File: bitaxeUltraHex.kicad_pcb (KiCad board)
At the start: 4 copper layers, 84.5 x 129.5 mm, 333 parts, among them J1 Conn_01x01, J2 Conn_01x01, J3 TC2030-IDC, J4 USB_C_Receptacle_USB2.0, J5 Conn_01x04, J6 Conn_01x04, Q1 NTMFS5C673NLT1G, Q2 CSD17577Q5A, Q3 NTMFS5C673NLT1G, Q4 CSD17577Q5A, Q5 BSS123, SW1 GT-TC029B-H025-L1N, SW2 GT-TC029B-H025-L1N, U1 uA7805, U10 TMP1075, U11 TMP1075, U12 EMC2302, U13 BM1366_mode1, U14 ADP171AUJ-R7, U15 ADP171AUJ-R7, U16 BM1366_mode1, U17 25MHz, U18 TLV3544, U19 BM1366_mode0, U2 RT9080-33GJ5, U20 ADP171AUJ-R7, U21 ADP171AUJ-R7, U22 BM1366_mode0, U23 TLV3544, U24 BM1366_mode1, U25 ADP171AUJ-R7, U26 ADP171AUJ-R7, U27 BM1366_mode1, U3 INA219AIDCNR, U4 TPS40305, U5 MIC5504, U6 DS4432U+, U7 SN74AVC4T774, U8 176x320_st7789, U9 ESP32-S3-WROOM-1, Y1 32.768kHz

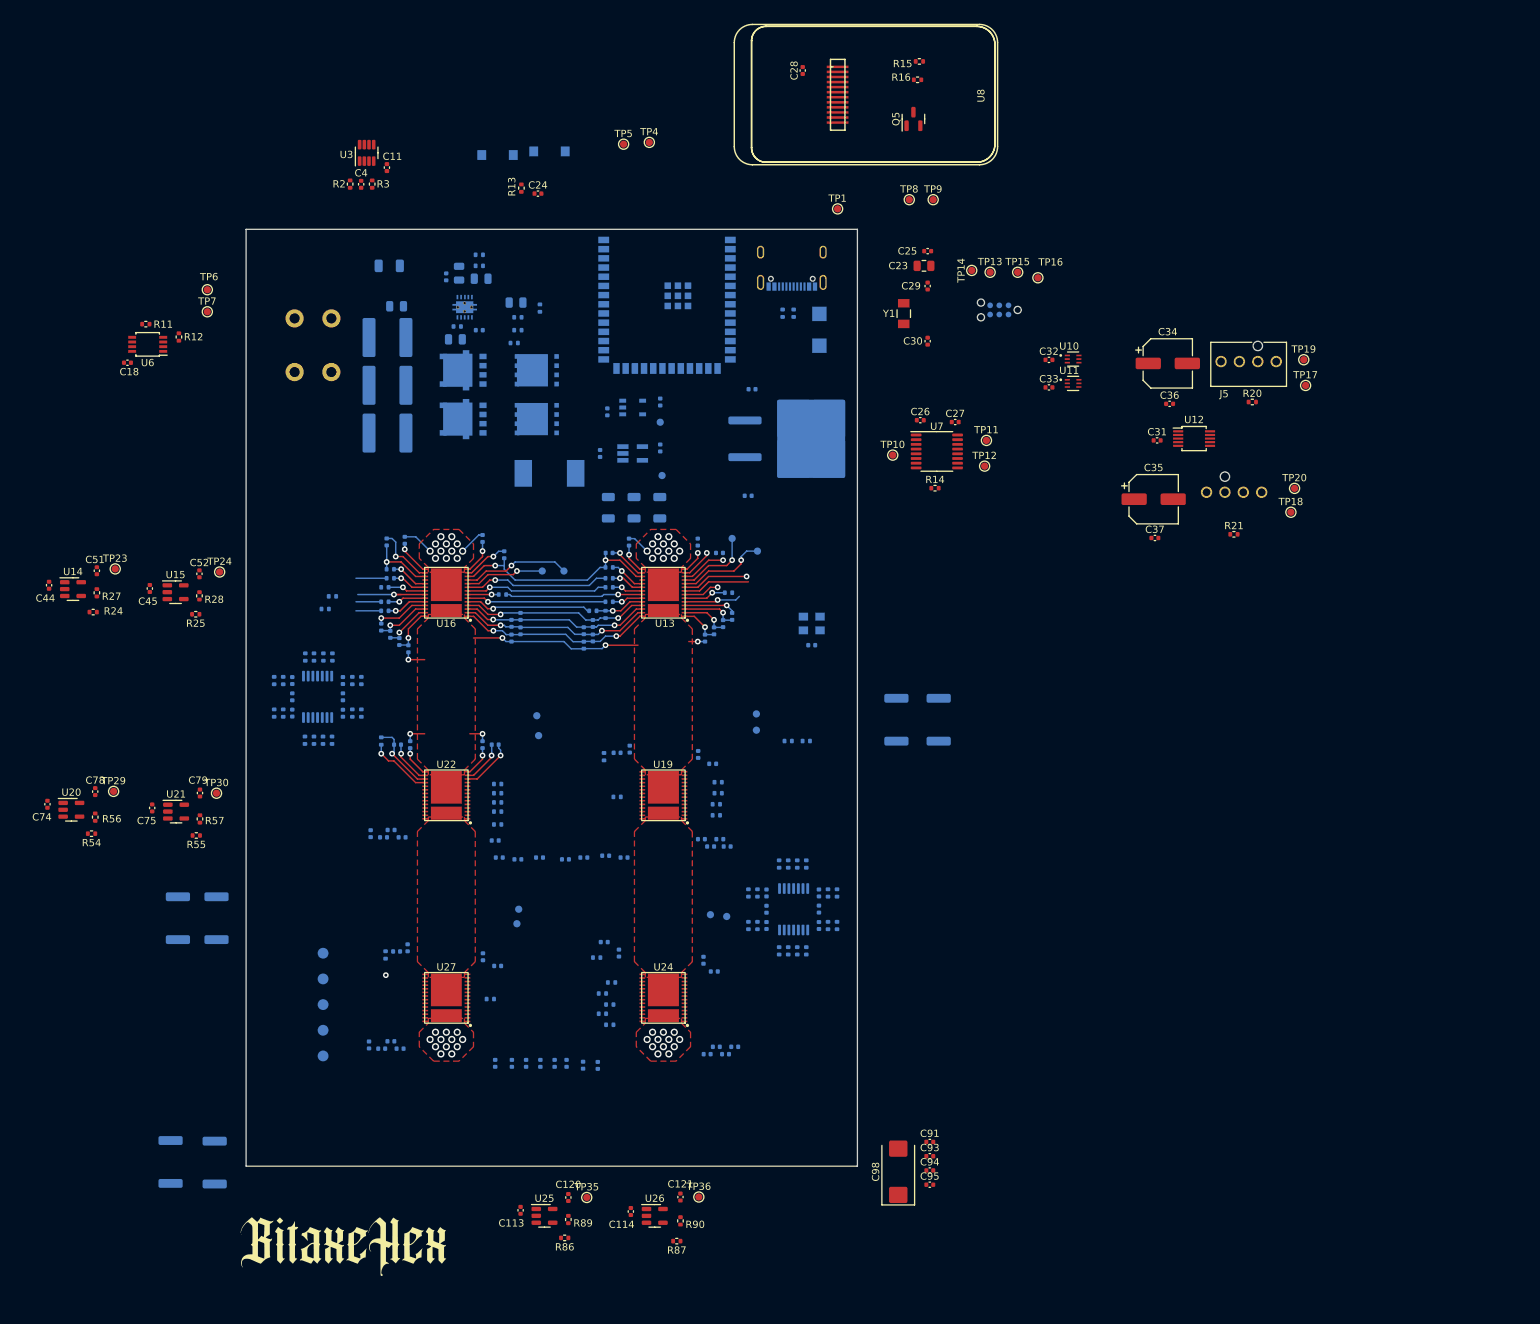
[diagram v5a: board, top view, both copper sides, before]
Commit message: move power resistors under ASICs
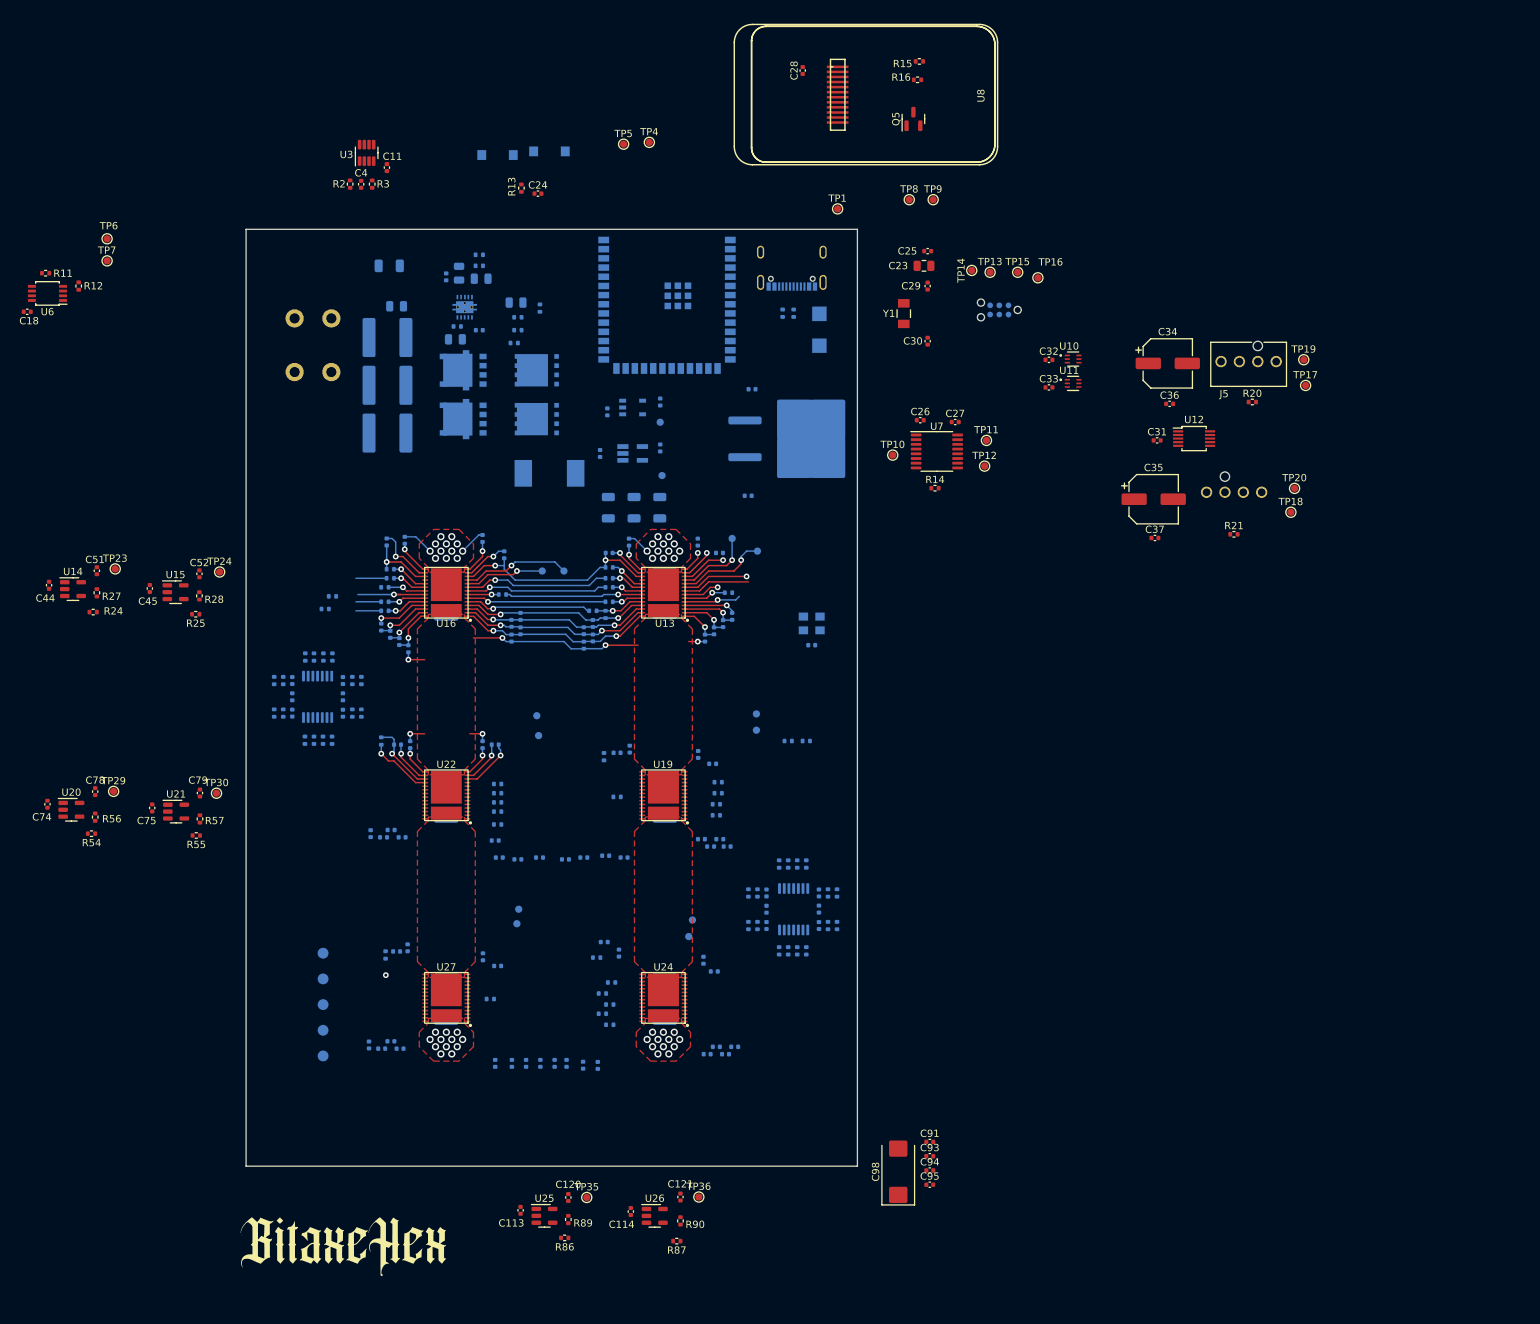
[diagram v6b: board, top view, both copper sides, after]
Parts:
- moved R99 71.9 mm to (108.2, 153.2)
- moved R35 70.2 mm to (78.0, 97.3)
- moved R68 69.4 mm to (108.2, 125.2)
- moved R98 39.2 mm to (78.0, 153.2)
- moved R34 36.5 mm to (108.2, 97.0)
- moved R62 35.9 mm to (78.0, 125.2)
- moved U6 15.5 mm to (22.9, 55.6)
- moved R12 15.5 mm to (27.2, 54.6)
- moved C18 15.5 mm to (20.1, 58.2)
- moved TP6 15.5 mm to (31.1, 48.1)
- moved R11 15.5 mm to (22.6, 52.8)
- moved TP7 15.5 mm to (31.1, 51.1)
- moved TP33 4.76 mm to (112.0, 142.2)
- moved TP34 4.26 mm to (111.5, 144.5)
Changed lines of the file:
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@@
   )
   (footprint "Package_SO:TSSOP-8_3x3mm_P0.65mm" (layer "F.Cu")
-    (at 36.712 62.667 180)
+    (at 22.86 55.626 180)
     (descr "TSSOP8: plastic thin shrink small outline package; 8 leads; body width 3 mm; (see NXP SSOP-TSSOP-VSO-REFLOW.pdf and sot505-1_po.pdf)")
     (tags "SSOP 0.65")
@@
   )
   (footprint "Capacitor_SMD:C_0402_1005Metric" (layer "F.Cu")
-    (at 33.918 65.207 180)
+    (at 20.066 58.166 180)
     (descr "Capacitor SMD 0402 (1005 Metric), square (rectangular) end terminal, IPC_7351 nominal, (Body size source: IPC-SM-782 page 76, https://www.pcb-3d.com/wordpress/wp-content/uploads/ipc-sm-782a_amendment_1_and_2.pdf), generated with kicad-footprint-generator")
     (tags "capacitor")
@@
   )
   (footprint "TestPoint:TestPoint_Pad_D1.0mm" (layer "F.Cu")
-    (at 44.958 55.118)
+    (at 31.106 48.077)
     (descr "SMD pad as test Point, diameter 1.0mm")
     (tags "test point SMD pad")
@@
   )
   (footprint "TestPoint:TestPoint_Pad_D1.0mm" (layer "F.Cu")
-    (at 44.958 58.168)
+    (at 31.106 51.127)
     (descr "SMD pad as test Point, diameter 1.0mm")
     (tags "test point SMD pad")
@@
   )
   (footprint "Resistor_SMD:R_0402_1005Metric" (layer "F.Cu")
-    (at 36.458 59.873)
+    (at 22.606 52.832)
     (descr "Resistor SMD 0402 (1005 Metric), square (rectangular) end terminal, IPC_7351 nominal, (Body size source: IPC-SM-782 page 72, https://www.pcb-3d.com/wordpress/wp-content/uploads/ipc-sm-782a_amendment_1_and_2.pdf), generated with kicad-footprint-generator")
     (tags "resistor")
@@
   )
   (footprint "Resistor_SMD:R_0402_1005Metric" (layer "F.Cu")
-    (at 41.03 61.651 90)
+    (at 27.178 54.61 90)
     (descr "Resistor SMD 0402 (1005 Metric), square (rectangular) end terminal, IPC_7351 nominal, (Body size source: IPC-SM-782 page 72, https://www.pcb-3d.com/wordpress/wp-content/uploads/ipc-sm-782a_amendment_1_and_2.pdf), generated with kicad-footprint-generator")
     (tags "resistor")
@@
   )
   (footprint "TestPoint:TestPoint_Pad_D1.0mm" (layer "B.Cu")
-    (at 116.75 141.75)
+    (at 112.014 142.24)
     (descr "SMD pad as test Point, diameter 1.0mm")
     (tags "test point SMD pad")
@@
     (property "ki_keywords" "test point tp")
     (attr exclude_from_pos_files exclude_from_bom)
-    (fp_text reference "TP33" (at 0 -2.54 90) (layer "B.SilkS")
+    (fp_text reference "TP33" (at -2.794 0 180) (layer "B.SilkS")
         (effects (font (size 1 1) (thickness 0.15)) (justify mirror))
     )
@@
   )
   (footprint "TestPoint:TestPoint_Pad_D1.0mm" (layer "B.Cu")
-    (at 114.5 141.5)
+    (at 111.506 144.526)
     (descr "SMD pad as test Point, diameter 1.0mm")
     (tags "test point SMD pad")
@@
     (property "ki_keywords" "test point tp")
     (attr exclude_from_pos_files exclude_from_bom)
-    (fp_text reference "TP34" (at 0 -2.54 90) (layer "B.SilkS")
+    (fp_text reference "TP34" (at -2.486 0.232 180) (layer "B.SilkS")
         (effects (font (size 1 1) (thickness 0.15)) (justify mirror))
     )
@@
   )
   (footprint "Resistor_SMD:R_2512_6332Metric" (layer "B.Cu")
-    (at 39.878 175.6825 90)
+    (at 108.204 153.162 90)
     (descr "Resistor SMD 2512 (6332 Metric), square (rectangular) end terminal, IPC_7351 nominal, (Body size source: IPC-SM-782 page 72, https://www.pcb-3d.com/wordpress/wp-content/uploads/ipc-sm-782a_amendment_1_and_2.pdf), generated with kicad-footprint-generator")
     (tags "resistor")
@@
     (property "ki_keywords" "R res resistor")
     (attr smd)
-    (fp_text reference "R99" (at -4.572 0) (layer "B.SilkS")
+    (fp_text reference "R99" (at 0.254 2.794 90) (layer "B.SilkS")
         (effects (font (size 1 1) (thickness 0.15)) (justify mirror))
     )
@@
   )
   (footprint "Resistor_SMD:R_2512_6332Metric" (layer "B.Cu")
-    (at 46.228 141.986 90)
+    (at 77.978 125.222 90)
     (descr "Resistor SMD 2512 (6332 Metric), square (rectangular) end terminal, IPC_7351 nominal, (Body size source: IPC-SM-782 page 72, https://www.pcb-3d.com/wordpress/wp-content/uploads/ipc-sm-782a_amendment_1_and_2.pdf), generated with kicad-footprint-generator")
     (tags "resistor")
@@
   )
   (footprint "Resistor_SMD:R_2512_6332Metric" (layer "B.Cu")
-    (at 45.974 175.768 90)
+    (at 77.978 153.162 90)
     (descr "Resistor SMD 2512 (6332 Metric), square (rectangular) end terminal, IPC_7351 nominal, (Body size source: IPC-SM-782 page 72, https://www.pcb-3d.com/wordpress/wp-content/uploads/ipc-sm-782a_amendment_1_and_2.pdf), generated with kicad-footprint-generator")
     (tags "resistor")
@@
     (property "ki_keywords" "R res resistor")
     (attr smd)
-    (fp_text reference "R98" (at -4.572 0) (layer "B.SilkS")
+    (fp_text reference "R98" (at 0 -2.54 90) (layer "B.SilkS")
         (effects (font (size 1 1) (thickness 0.15)) (justify mirror))
     )
@@
   )
   (footprint "Resistor_SMD:R_2512_6332Metric" (layer "B.Cu")
-    (at 146.05 114.554 90)
+    (at 77.978 97.282 90)
     (descr "Resistor SMD 2512 (6332 Metric), square (rectangular) end terminal, IPC_7351 nominal, (Body size source: IPC-SM-782 page 72, https://www.pcb-3d.com/wordpress/wp-content/uploads/ipc-sm-782a_amendment_1_and_2.pdf), generated with kicad-footprint-generator")
     (tags "resistor")
@@
     (property "ki_keywords" "R res resistor")
     (attr smd)
-    (fp_text reference "R35" (at 4.572 0) (layer "B.SilkS")
+    (fp_text reference "R35" (at -0.254 -2.54 90) (layer "B.SilkS")
         (effects (font (size 1 1) (thickness 0.15)) (justify mirror))
     )
@@
     (property "ki_keywords" "test point tp")
     (attr exclude_from_pos_files exclude_from_bom)
-    (fp_text reference "TP37" (at -3 0) (layer "B.SilkS")
+    (fp_text reference "TP37" (at 2.674 0) (layer "B.SilkS")
         (effects (font (size 1 1) (thickness 0.15)) (justify mirror))
     )
@@
   )
   (footprint "Resistor_SMD:R_2512_6332Metric" (layer "B.Cu")
-    (at 140.208 114.554 90)
+    (at 108.204 97.028 90)
     (descr "Resistor SMD 2512 (6332 Metric), square (rectangular) end terminal, IPC_7351 nominal, (Body size source: IPC-SM-782 page 72, https://www.pcb-3d.com/wordpress/wp-content/uploads/ipc-sm-782a_amendment_1_and_2.pdf), generated with kicad-footprint-generator")
     (tags "resistor")
@@
     (property "ki_keywords" "R res resistor")
     (attr smd)
-    (fp_text reference "R34" (at 4.572 0) (layer "B.SilkS")
+    (fp_text reference "R34" (at 0 2.54 90) (layer "B.SilkS")
         (effects (font (size 1 1) (thickness 0.15)) (justify mirror))
     )
@@
   )
   (footprint "Resistor_SMD:R_2512_6332Metric" (layer "B.Cu")
-    (at 40.894 141.986 90)
+    (at 108.204 125.222 90)
     (descr "Resistor SMD 2512 (6332 Metric), square (rectangular) end terminal, IPC_7351 nominal, (Body size source: IPC-SM-782 page 72, https://www.pcb-3d.com/wordpress/wp-content/uploads/ipc-sm-782a_amendment_1_and_2.pdf), generated with kicad-footprint-generator")
     (tags "resistor")
@@
     (property "ki_keywords" "test point tp")
     (attr exclude_from_pos_files exclude_from_bom)
-    (fp_text reference "TP38" (at -3 0) (layer "B.SilkS")
+    (fp_text reference "TP38" (at 2.678 -0.034) (layer "B.SilkS")
         (effects (font (size 1 1) (thickness 0.15)) (justify mirror))
     )

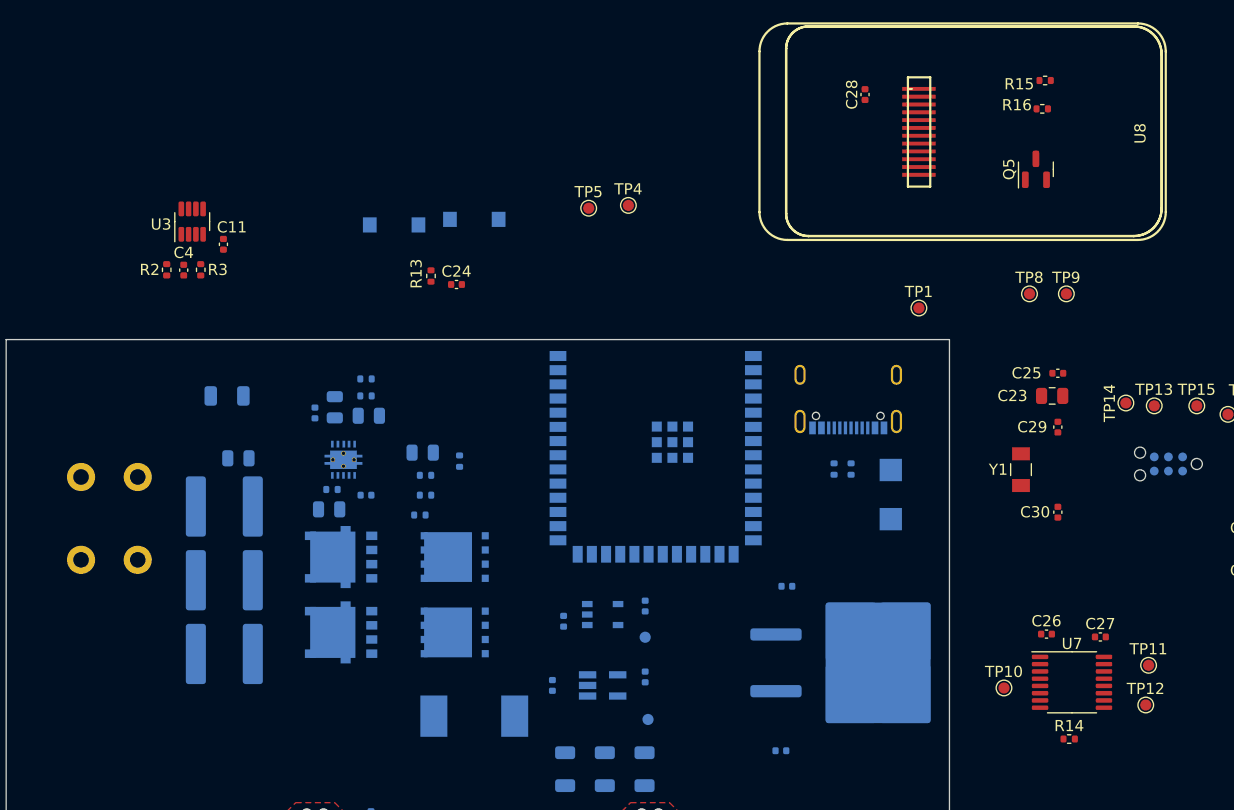
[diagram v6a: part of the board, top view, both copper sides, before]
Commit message: add screw terminals, replace OLED display with optional connector
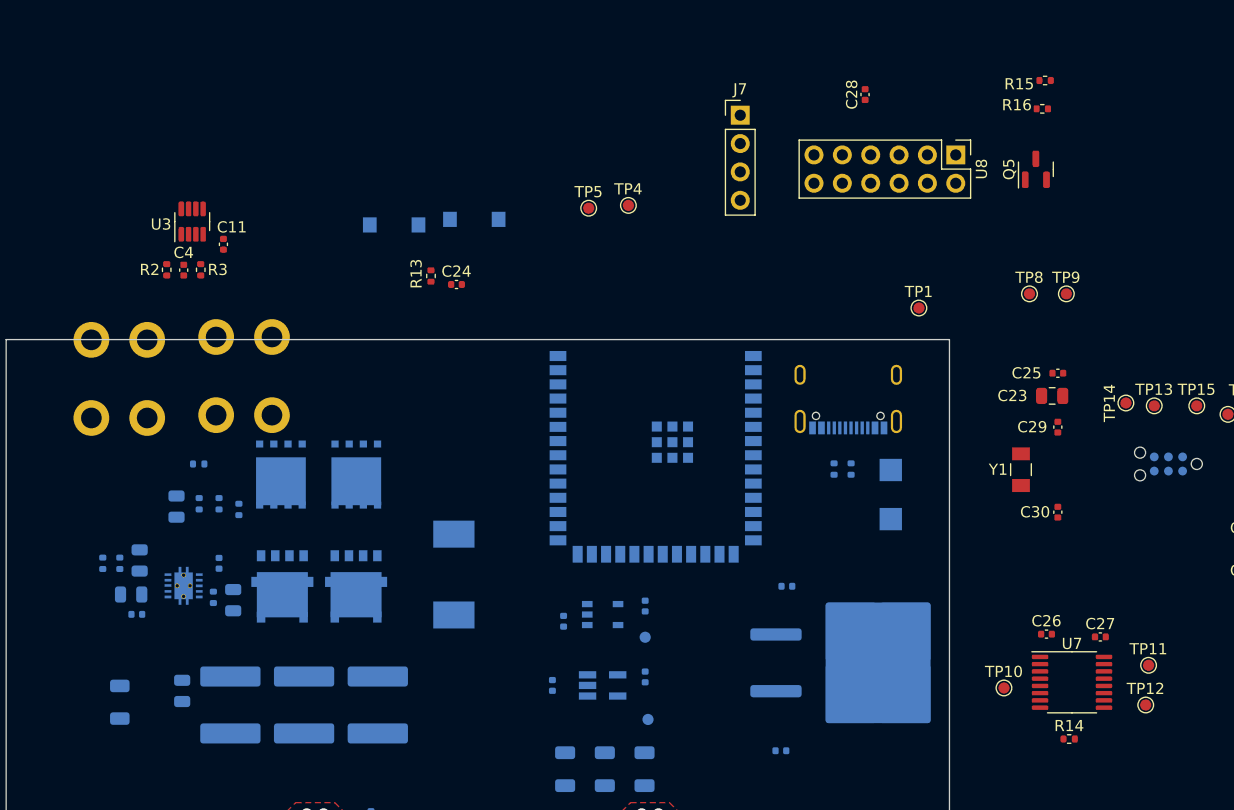
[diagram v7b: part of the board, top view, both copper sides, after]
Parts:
- added J7: Conn_01x04, Connector_PinHeader_2.54mm:PinHeader_1x04_P2.54mm_Vertical, F.Cu at (116.1, 26.7)
- J1, J2: footprint bitaxe:63862-1 -> bitaxe:7770-screw-terminal
- U8: footprint bitaxe:ST7789-176x320 -> Connector_PinHeader_2.54mm:PinHeader_2x06_P2.54mm_Vertical
- moved U8 36.5 mm to (135.4, 30.2)
- moved R1 29.1 mm to (60.5, 79.3), turned to 90 degrees
- moved R7 28.8 mm to (59.0, 66.8), turned to -90 degrees
- moved R4 26.7 mm to (60.5, 66.8), turned to 90 degrees
- moved C9 24.8 mm to (61.5, 69.6), turned to 180 degrees
- moved C7 24.3 mm to (62.3, 66.6), turned to 90 degrees
- moved C10 24.1 mm to (62.0, 71.4), turned to 180 degrees
- moved R8 23.4 mm to (67.6, 57.9), turned to 180 degrees
- moved C19 22.6 mm to (65.6, 61.7), turned to -90 degrees
- moved C8 21.4 mm to (66.1, 78.2), turned to -90 degrees
- moved R9 20.4 mm to (67.6, 61.5), turned to -90 degrees
- moved R10 18.5 mm to (69.4, 61.5), turned to 90 degrees
- moved U4 18.2 mm to (66.2, 68.8), turned to 0 degrees
- moved C1 17.8 mm to (70.4, 79.5), turned to -90 degrees
- moved Q2 17.2 mm to (74.9, 58.9), turned to -90 degrees
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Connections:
- U2 pad 4: (no net) -> unconnected-(U2-NC-Pad4)
